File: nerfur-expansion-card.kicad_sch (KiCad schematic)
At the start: 12 parts, among them J1 RJ45, J10 AudioJack4, J11 HDMI_A, J2 Micro_SD_Card, J3 RJ45, J4 Micro_SD_Card, J5 USB_A, J6 USB_A, J7 USB_A, J8 HDMI_A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

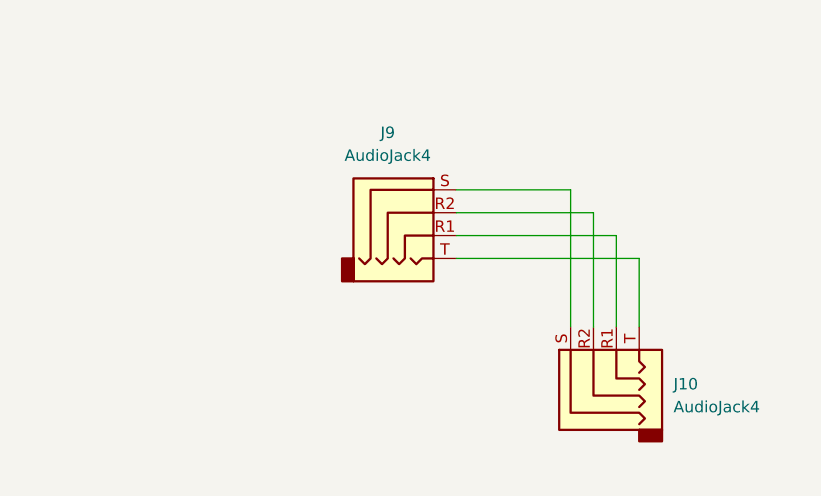
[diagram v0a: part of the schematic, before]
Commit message: Assigned footprints
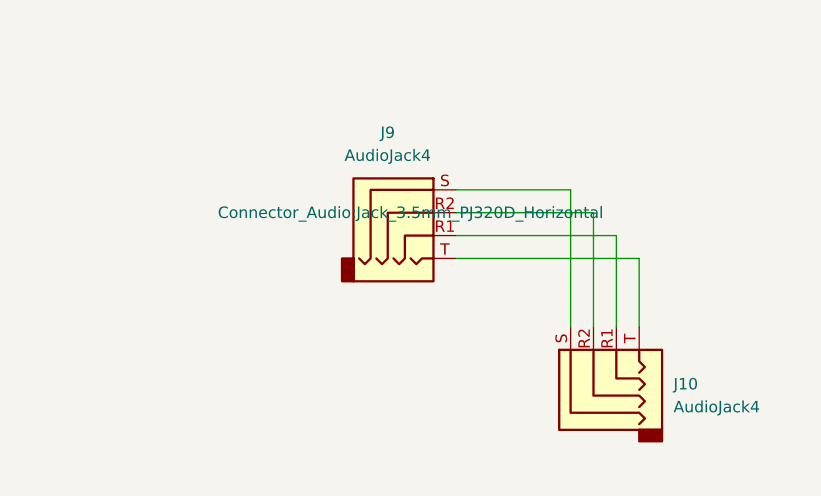
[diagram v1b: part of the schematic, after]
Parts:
- J1, J3: footprint (none) -> Connector_RJ:RJ45_OST_PJ012-8P8CX_Vertical
- J10: footprint (none) -> Connector_Audio:Jack_3.5mm_PJ320D_Horizontal
- J11, J8: footprint (none) -> Connector_Video:HDMI_A_Molex_208658-1001_Horizontal
- J2, J4: footprint (none) -> Connector_Card:microSD_HC_Molex_47219-2001
- J5, J6, J7: footprint (none) -> Connector_USB:USB_A_Molex_67643_Horizontal
- J9: footprint Connector_Audio:Jack_3.5mm_CUI_SJ-3523-SMT_Horizontal -> Connector_Audio:Jack_3.5mm_PJ320D_Horizontal
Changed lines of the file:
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@@
 			)
 		)
-		(property "Footprint" ""
+		(property "Footprint" "Connector_RJ:RJ45_OST_PJ012-8P8CX_Vertical"
 			(at 79.375 81.28 90)
 			(effects
@@
 			)
 		)
-		(property "Footprint" ""
+		(property "Footprint" "Connector_Video:HDMI_A_Molex_208658-1001_Horizontal"
 			(at 355.6 213.995 0)
 			(effects
@@
 			)
 		)
-		(property "Footprint" ""
+		(property "Footprint" "Connector_USB:USB_A_Molex_67643_Horizontal"
 			(at 176.53 60.96 0)
 			(effects
@@
 			)
 		)
-		(property "Footprint" ""
+		(property "Footprint" "Connector_USB:USB_A_Molex_67643_Horizontal"
 			(at 213.36 209.55 0)
 			(effects
@@
 			)
 		)
-		(property "Footprint" "Connector_Audio:Jack_3.5mm_CUI_SJ-3523-SMT_Horizontal"
+		(property "Footprint" "Connector_Audio:Jack_3.5mm_PJ320D_Horizontal"
 			(at 314.96 60.96 0)
 			(effects
@@
 					(size 1.27 1.27)
 				)
-				(hide yes)
 			)
 		)
@@
 			)
 		)
-		(property "Footprint" ""
+		(property "Footprint" "Connector_Card:microSD_HC_Molex_47219-2001"
 			(at 120.65 243.84 0)
 			(effects
@@
 			)
 		)
-		(property "Footprint" ""
+		(property "Footprint" "Connector_Video:HDMI_A_Molex_208658-1001_Horizontal"
 			(at 288.925 181.61 0)
 			(effects
@@
 			)
 		)
-		(property "Footprint" ""
+		(property "Footprint" "Connector_Audio:Jack_3.5mm_PJ320D_Horizontal"
 			(at 335.28 78.74 0)
 			(effects
@@
 			)
 		)
-		(property "Footprint" ""
+		(property "Footprint" "Connector_Card:microSD_HC_Molex_47219-2001"
 			(at 21.59 187.96 0)
 			(effects
@@
 			)
 		)
-		(property "Footprint" ""
+		(property "Footprint" "Connector_USB:USB_A_Molex_67643_Horizontal"
 			(at 200.66 76.2 0)
 			(effects
@@
 			)
 		)
-		(property "Footprint" ""
+		(property "Footprint" "Connector_RJ:RJ45_OST_PJ012-8P8CX_Vertical"
 			(at 49.53 57.785 90)
 			(effects
